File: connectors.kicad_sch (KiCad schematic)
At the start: 4 parts, among them J1 Conn_01x04_Pin, J2 Conn_01x04_Pin, J3 Conn_01x09_Pin, J4 Conn_02x03_Odd_Even

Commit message: proceeded to wire all the components on the first sheet
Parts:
- J1, J2: footprint (none) -> Connector_PinHeader_2.54mm:PinHeader_1x04_P2.54mm_Vertical
- J3: footprint (none) -> Connector_PinHeader_2.54mm:PinHeader_1x09_P2.54mm_Vertical
- J4: footprint (none) -> Connector_PinHeader_2.54mm:PinHeader_2x03_P2.54mm_Vertical
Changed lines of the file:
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@@
 			)
 		)
-		(property "Footprint" ""
+		(property "Footprint" "Connector_PinHeader_2.54mm:PinHeader_1x04_P2.54mm_Vertical"
 			(at 156.21 55.88 0)
 			(effects
@@
 			)
 		)
-		(property "Footprint" ""
+		(property "Footprint" "Connector_PinHeader_2.54mm:PinHeader_1x09_P2.54mm_Vertical"
 			(at 196.85 62.23 0)
 			(effects
@@
 			)
 		)
-		(property "Footprint" ""
+		(property "Footprint" "Connector_PinHeader_2.54mm:PinHeader_2x03_P2.54mm_Vertical"
 			(at 160.02 83.82 0)
 			(effects
@@
 			)
 		)
-		(property "Footprint" ""
+		(property "Footprint" "Connector_PinHeader_2.54mm:PinHeader_1x04_P2.54mm_Vertical"
 			(at 176.53 55.88 0)
 			(effects

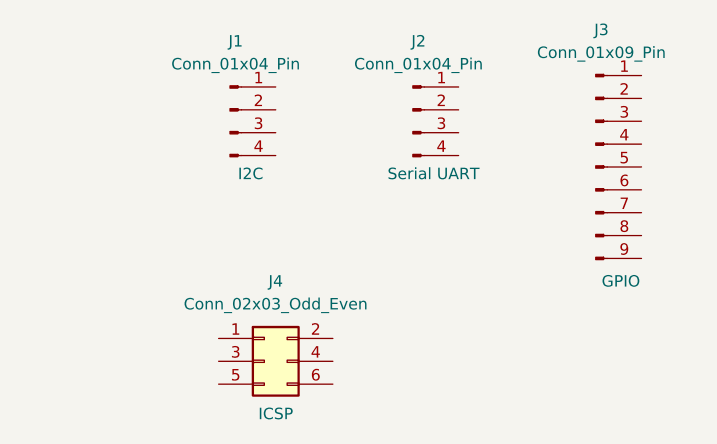
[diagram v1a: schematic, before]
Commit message: the sheet is fully wired ready for an ERC
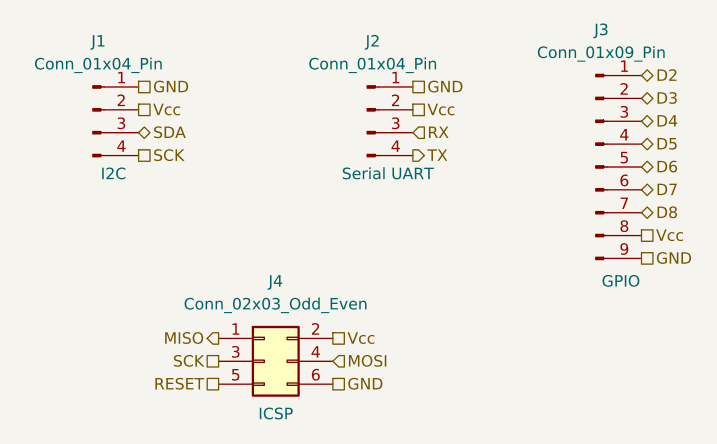
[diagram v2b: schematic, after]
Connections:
- net GND: now reaches J1.1 (Pin_1)
- net GND: now also J2.1 (Pin_1), J3.9 (Pin_9), J4.6 (Pin_6)
- net Vcc: now reaches J1.2 (Pin_2)
- net Vcc: now also J2.2 (Pin_2), J3.8 (Pin_8), J4.2 (Pin_2)
- net SDA: now reaches J1.3 (Pin_3)
- net SCK: now reaches J1.4 (Pin_4)
- net SCK: now also J4.3 (Pin_3)
- net D2: now reaches J3.1 (Pin_1)
- net D3: now reaches J3.2 (Pin_2)
- net D4: now reaches J3.3 (Pin_3)
- net D5: now reaches J3.4 (Pin_4)
- net D6: now reaches J3.5 (Pin_5)
- net D7: now reaches J3.6 (Pin_6)
- net D8: now reaches J3.7 (Pin_7)
- net MISO: now reaches J4.1 (Pin_1)
- net MOSI: now reaches J4.4 (Pin_4)
- net RESET: now reaches J4.5 (Pin_5)
- net RX: now reaches J2.3 (Pin_3)
- net TX: now reaches J2.4 (Pin_4)
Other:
- moved on the sheet: J1, J2

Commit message: finished an improved version of the 2 layer PCB
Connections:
- net SCK: no longer J1.4 (Pin_4)
- new net SCL: J1.4 (Pin_4)
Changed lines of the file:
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@@
 		)
 	)
-	(hierarchical_label "SCK"
+	(hierarchical_label "SCL"
 		(shape passive)
 		(at 146.05 60.96 0)
